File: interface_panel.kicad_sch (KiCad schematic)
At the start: 49 parts, among them J1 Conn_01x04_Pin, J5 Led, J7 Conn_02x05_Odd_Even, J8 `, Q1 BC547, Q2 BC547, U1 SM420561N, U2 ATmega328P-P, U4 SM420561N, U7 TTP223-BA6, U8 TTP223-BA6, U9 TTP223-BA6, Y1 Crystal

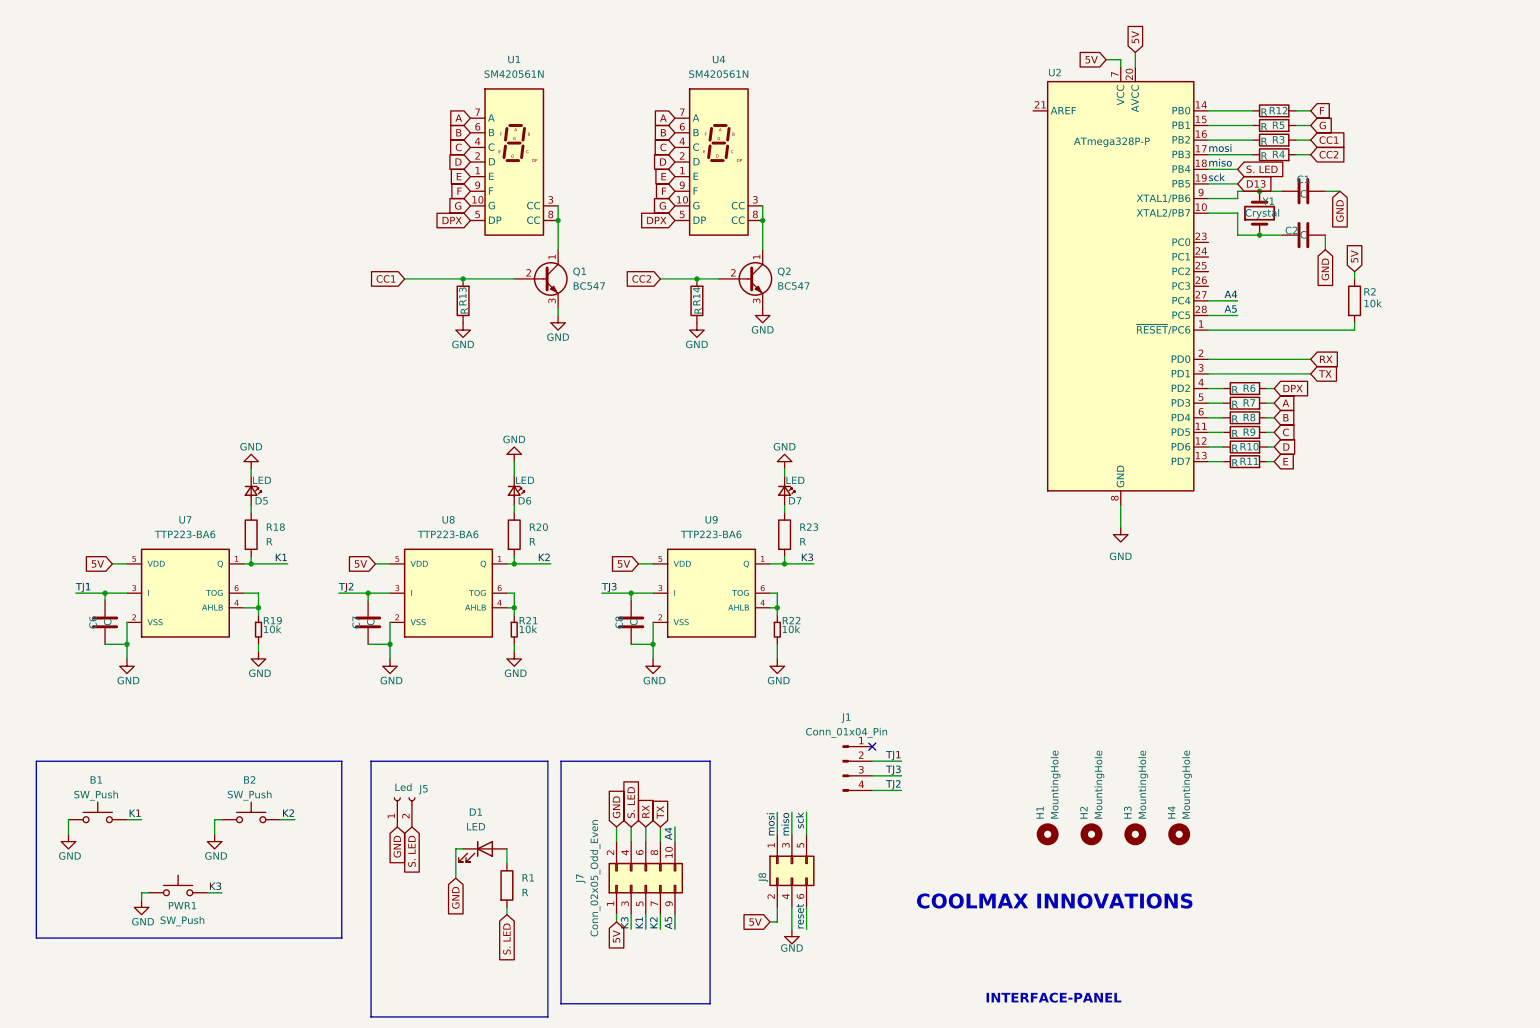
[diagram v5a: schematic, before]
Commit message: unrouted tracks - A4,A5
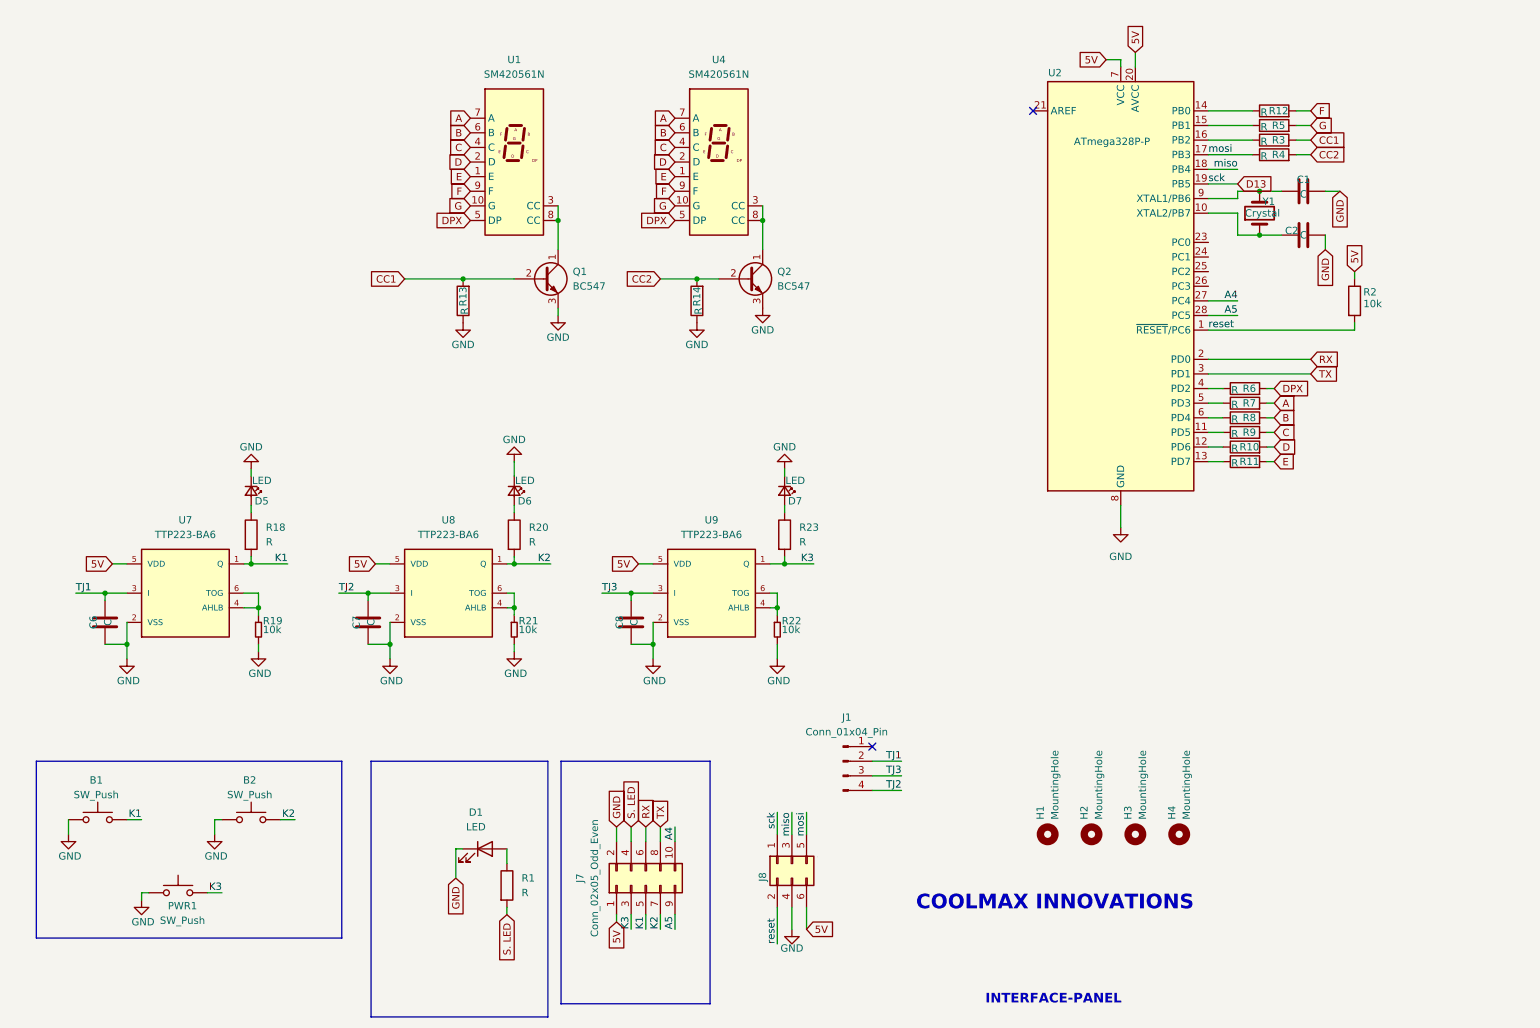
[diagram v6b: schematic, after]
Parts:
- removed J5: Led, Connector_JST:JST_EH_B2B-EH-A_1x02_P2.50mm_Vertical, symbol Connector:Conn_01x02_Socket
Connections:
- net 5V: now also J8.6 (Pin_6); no longer J8.2 (Pin_2)
- net D13: now also J8.1 (Pin_1); no longer J8.5 (Pin_5)
- net S. LED: no longer J8.3 (Pin_3), U2.18 (PB4)
- net mosi: now also J8.5 (Pin_5); no longer J8.1 (Pin_1)
- net reset: now also J8.2 (Pin_2), R2.2, U2.1 (~{RESET}/PC6); no longer J8.6 (Pin_6)
- new net miso: J8.3 (Pin_3), U2.18 (PB4)
- no-connect marks 1 -> 2
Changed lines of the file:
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@@
 		)
 	)
-	(rectangle
-		(start 86.36 158.75)
-		(end 86.36 158.75)
-		(stroke
-			(width 0)
-			(type default)
-		)
-		(fill
-			(type none)
-		)
-	)
 	(text "INTERFACE-PANEL\n"
 		(exclude_from_sim no)
@@
 		(at 170.18 146.05)
 	)
+	(no_connect
+		(at 198.12 35.56)
+	)
 	(wire
 		(pts
@@
 	(wire
 		(pts
+			(xy 233.68 45.72) (xy 228.6 45.72)
+		)
+		(stroke
+			(width 0)
+			(type default)
+		)
+	)
+	(wire
+		(pts
 			(xy 57.15 171.45) (xy 54.61 171.45)
 		)
@@
 	(wire
 		(pts
-			(xy 152.4 176.53) (xy 153.67 176.53)
-		)
-		(stroke
-			(width 0)
-			(type default)
-		)
-	)
-	(wire
-		(pts
 			(xy 69.85 158.75) (xy 67.31 158.75)
 		)
@@
 	(wire
 		(pts
-			(xy 153.67 176.53) (xy 153.67 173.99)
+			(xy 153.67 173.99) (xy 153.67 180.34)
 		)
 		(stroke
@@
 	(wire
 		(pts
-			(xy 228.6 45.72) (xy 233.68 45.72)
-		)
-		(stroke
-			(width 0)
-			(type default)
-		)
-	)
-	(wire
-		(pts
 			(xy 99.06 64.77) (xy 107.95 64.77)
 		)
@@
 		)
 	)
-	(label "mosi"
-		(at 153.67 157.48 270)
-		(effects
-			(font
-				(size 1.27 1.27)
-			)
-			(justify right bottom)
-		)
-	)
-	(label "sck"
-		(at 158.75 157.48 270)
+	(label "A4"
+		(at 135.89 160.02 270)
 		(effects
 			(font
@@
 		)
 	)
-	(label "A4"
-		(at 135.89 160.02 270)
+	(label "reset"
+		(at 153.67 180.34 90)
 		(effects
 			(font
 				(size 1.27 1.27)
 			)
-			(justify right bottom)
+			(justify left bottom)
 		)
 	)
@@
 		)
 	)
-	(label "K2"
-		(at 133.35 177.8 90)
+	(label "mosi"
+		(at 158.75 157.48 270)
 		(effects
 			(font
 				(size 1.27 1.27)
 			)
-			(justify left bottom)
+			(justify right bottom)
 		)
 	)
-	(label "miso"
-		(at 156.21 157.48 270)
+	(label "sck"
+		(at 153.67 157.48 270)
 		(effects
 			(font
@@
 		)
 	)
+	(label "K2"
+		(at 133.35 177.8 90)
+		(effects
+			(font
+				(size 1.27 1.27)
+			)
+			(justify left bottom)
+		)
+	)
 	(label "K1"
 		(at 68.58 114.3 180)
@@
 	)
 	(label "reset"
-		(at 158.75 177.8 90)
+		(at 228.6 73.66 0)
 		(effects
 			(font
@@
 	)
 	(label "miso"
-		(at 228.6 45.72 0)
+		(at 233.68 45.72 180)
 		(effects
 			(font
 				(size 1.27 1.27)
 			)
-			(justify left bottom)
+			(justify right bottom)
 		)
 	)
@@
 		)
 	)
+	(label "miso"
+		(at 156.21 157.48 270)
+		(effects
+			(font
+				(size 1.27 1.27)
+			)
+			(justify right bottom)
+		)
+	)
 	(label "TJ3"
 		(at 175.26 151.13 180)
@@
 		)
 	)
-	(global_label "S. LED"
-		(shape input)
-		(at 233.68 45.72 0)
-		(fields_autoplaced yes)
-		(effects
-			(font
-				(size 1.27 1.27)
-			)
-			(justify left)
-		)
-		(property "Intersheetrefs" "${INTERSHEET_REFS}"
-			(at 242.8942 45.72 0)
-			(effects
-				(font
-					(size 1.27 1.27)
-				)
-				(justify left)
-				(hide yes)
-			)
-		)
-	)
 	(global_label "RX"
 		(shape input)
@@
 	(global_label "5V"
 		(shape input)
-		(at 38.1 114.3 180)
+		(at 158.75 177.8 0)
 		(fields_autoplaced yes)
 		(effects
@@
 				(size 1.27 1.27)
 			)
-			(justify right)
+			(justify left)
 		)
 		(property "Intersheetrefs" "${INTERSHEET_REFS}"
-			(at 32.8167 114.3 0)
+			(at 164.0333 177.8 0)
 			(effects
 				(font
 					(size 1.27 1.27)
 				)
-				(justify right)
+				(justify left)
 				(hide yes)
 			)
@@
 	(global_label "5V"
 		(shape input)
-		(at 152.4 176.53 180)
+		(at 38.1 114.3 180)
 		(fields_autoplaced yes)
 		(effects
@@
 		)
 		(property "Intersheetrefs" "${INTERSHEET_REFS}"
-			(at 147.1167 176.53 0)
+			(at 32.8167 114.3 0)
 			(effects
 				(font
@@
 		)
 	)
-	(global_label "GND"
-		(shape input)
-		(at 87.63 160.02 270)
-		(fields_autoplaced yes)
-		(effects
-			(font
-				(size 1.27 1.27)
-			)
-			(justify right)
-		)
-		(property "Intersheetrefs" "${INTERSHEET_REFS}"
-			(at 87.63 166.8757 90)
-			(effects
-				(font
-					(size 1.27 1.27)
-				)
-				(justify right)
-				(hide yes)
-			)
-		)
-	)
 	(global_label "D"
 		(shape input)
@@
 		)
 	)
-	(global_label "S. LED"
-		(shape input)
-		(at 90.17 160.02 270)
-		(fields_autoplaced yes)
-		(effects
-			(font
-				(size 1.27 1.27)
-			)
-			(justify right)
-		)
-		(property "Intersheetrefs" "${INTERSHEET_REFS}"
-			(at 90.17 169.2342 90)
-			(effects
-				(font
-					(size 1.27 1.27)
-				)
-				(justify right)
-				(hide yes)
-			)
-		)
-	)
 	(global_label "G"
 		(shape input)
@@
 					(unit 1)
 				)
-			)
-		)
-	)
-	(symbol
-		(lib_id "Connector:Conn_01x02_Socket")
-		(at 87.63 154.94 90)
-		(unit 1)
-		(exclude_from_sim no)
-		(in_bom yes)
-		(on_board yes)
-		(dnp no)
-		(property "Reference" "J5"
-			(at 91.44 153.416 90)
-			(effects
-				(font
-					(size 1.27 1.27)
-				)
-				(justify right)
-			)
-		)
-		(property "Value" "Led"
-			(at 87.122 153.162 90)
-			(effects
-				(font
-					(size 1.27 1.27)
-				)
-				(justify right)
-			)
-		)
-		(property "Footprint" "Connector_JST:JST_EH_B2B-EH-A_1x02_P2.50mm_Vertical"
-			(at 87.63 154.94 0)
-			(effects
-				(font
-					(size 1.27 1.27)
-				)
-				(hide yes)
-			)
-		)
-		(property "Datasheet" "~"
-			(at 87.63 154.94 0)
-			(effects
-				(font
-					(size 1.27 1.27)
-				)
-				(hide yes)
-			)
-		)
-		(property "Description" "Generic connector, single row, 01x02, script generated"
-			(at 87.63 154.94 0)
-			(effects
-				(font
-					(size 1.27 1.27)
-				)
-				(hide yes)
-			)
-		)
-		(pin "2"
-		)
-		(pin "1"
-		)
-		(instances
-			(project "interface_panel"
-				(path "/9f0ac2f5-026e-46a7-84a3-e69ffa4f4cba"
-					(reference "J5")
-					(unit 1)
-				)

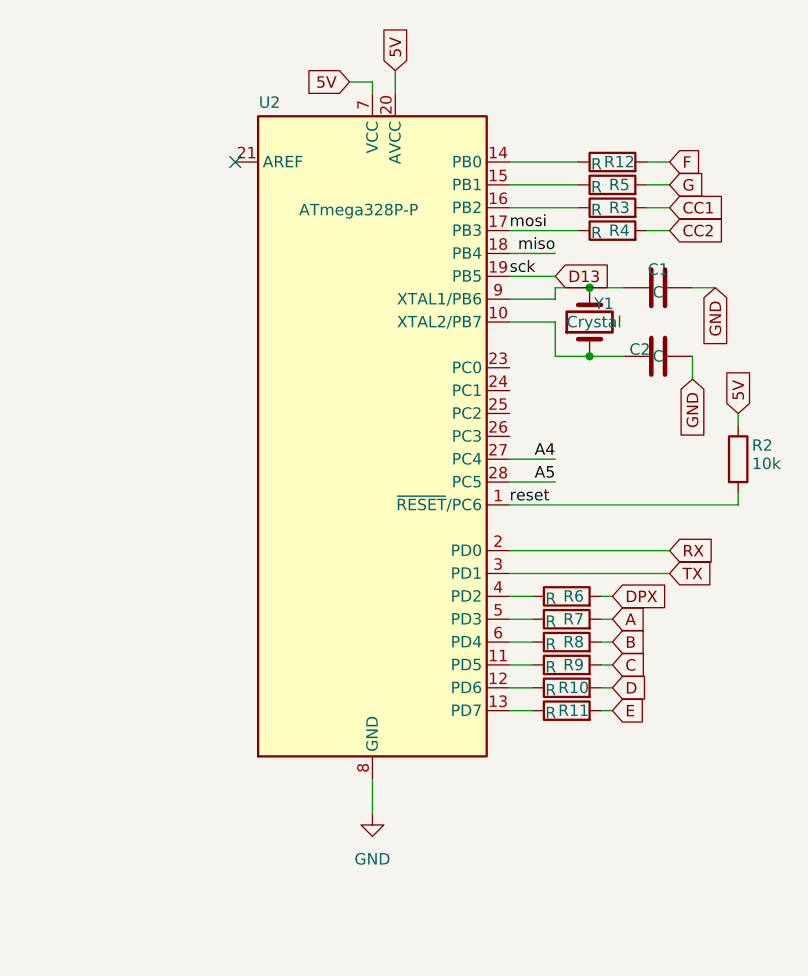
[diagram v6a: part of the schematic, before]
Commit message: Fixed- schematics -atmega symbol
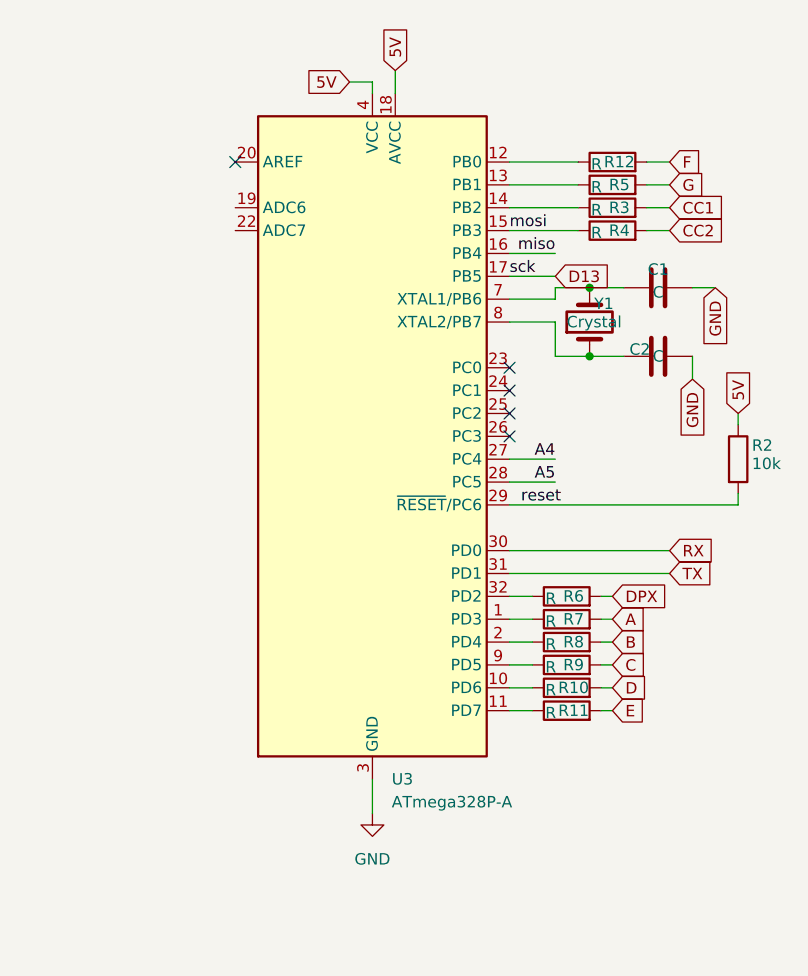
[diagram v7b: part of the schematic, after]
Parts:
- removed U2: ATmega328P-P, atmega328p-smd:QFP80P900X900X120-32N, symbol MCU_Microchip_ATmega:ATmega328P-P
- added U3: ATmega328P-A, Package_QFP:TQFP-32_7x7mm_P0.8mm, symbol MCU_Microchip_ATmega:ATmega328P-A
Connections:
- net 5V: now also U3.18 (AVCC), U3.4 (VCC), U3.6 (VCC)
- net A4: now also U3.27 (PC4)
- net A5: now also U3.28 (PC5)
- net D13: now also U3.17 (PB5)
- net GND: now also U3.21 (GND), U3.3 (GND), U3.5 (GND)
- net RX: now also U3.30 (PD0)
- net TX: now also U3.31 (PD1)
- net miso: now also U3.16 (PB4)
- net mosi: now also U3.15 (PB3)
- net reset: now also U3.29 (~{RESET}/PC6)
- net at R5.1: now also U3.13 (PB1)
- net at C1.1, Y1.2: now also U3.7 (XTAL1/PB6)
- net at R11.1: now also U3.11 (PD7)
- net at R7.1: now also U3.1 (PD3)
- net at R8.1: now also U3.2 (PD4)
- net at R10.1: now also U3.10 (PD6)
- net at R3.1: now also U3.14 (PB2)
- net at R9.1: now also U3.9 (PD5)
- net at C2.1, Y1.1: now also U3.8 (XTAL2/PB7)
- net at R12.1: now also U3.12 (PB0)
- net at R6.1: now also U3.32 (PD2)
- no-connect marks 2 -> 6
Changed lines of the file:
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@@
 	)
 	(no_connect
+		(at 228.6 60.96)
+	)
+	(no_connect
 		(at 170.18 146.05)
 	)
 	(no_connect
+		(at 228.6 66.04)
+	)
+	(no_connect
 		(at 198.12 35.56)
 	)
+	(no_connect
+		(at 228.6 58.42)
+	)
+	(no_connect
+		(at 228.6 63.5)
+	)
 	(wire
 		(pts
@@
 	(wire
 		(pts
+			(xy 228.6 73.66) (xy 254 73.66)
+		)
+		(stroke
+			(width 0)
+			(type default)
+		)
+	)
+	(wire
+		(pts
 			(xy 151.13 54.61) (xy 151.13 59.69)
 		)
@@
 	(wire
 		(pts
-			(xy 228.6 73.66) (xy 254 73.66)
-		)
-		(stroke
-			(width 0)
-			(type default)
-		)
-	)
-	(wire
-		(pts
 			(xy 158.75 157.48) (xy 158.75 161.29)
 		)
@@
 	)
 	(label "reset"
-		(at 228.6 73.66 0)
+		(at 229.87 73.66 0)
 		(effects
 			(font
@@
 	)
 	(symbol
+		(lib_id "MCU_Microchip_ATmega:ATmega328P-A")
+		(at 213.36 66.04 0)
+		(unit 1)
+		(exclude_from_sim no)
+		(in_bom yes)
+		(on_board yes)
+		(dnp no)
+		(fields_autoplaced yes)
+		(property "Reference" "U3"
+			(at 215.5033 104.14 0)
+			(effects
+				(font
+					(size 1.27 1.27)
+				)
+				(justify left)
+			)
+		)
+		(property "Value" "ATmega328P-A"
+			(at 215.5033 106.68 0)
+			(effects
+				(font
+					(size 1.27 1.27)
+				)
+				(justify left)
+			)
+		)
+		(property "Footprint" "Package_QFP:TQFP-32_7x7mm_P0.8mm"
+			(at 213.36 66.04 0)
+			(effects
+				(font
+					(size 1.27 1.27)
+					(italic yes)
+				)
+				(hide yes)
+			)
+		)
+		(property "Datasheet" "http://ww1.microchip.com/downloads/en/DeviceDoc/ATmega328_P%20AVR%20MCU%20with%20picoPower%20Technology%20Data%20Sheet%2040001984A.pdf"
+			(at 213.36 66.04 0)
+			(effects
+				(font
+					(size 1.27 1.27)
+				)
+				(hide yes)
+			)
+		)
+		(property "Description" "20MHz, 32kB Flash, 2kB SRAM, 1kB EEPROM, TQFP-32"
+			(at 213.36 66.04 0)
+			(effects
+				(font
+					(size 1.27 1.27)
+				)
+				(hide yes)
+			)
+		)
+		(pin "26"
+		)
+		(pin "14"
+		)
+		(pin "16"
+		)
+		(pin "31"
+		)
+		(pin "28"
+		)
+		(pin "1"
+		)
+		(pin "21"
+		)
+		(pin "32"
+		)
+		(pin "3"
+		)
+		(pin "18"
+		)
+		(pin "13"
+		)
+		(pin "25"
+		)
+		(pin "20"
+		)
+		(pin "5"
+		)
+		(pin "23"
+		)
+		(pin "15"
+		)
+		(pin "19"
+		)
+		(pin "8"
+		)
+		(pin "4"
+		)
+		(pin "6"
+		)
+		(pin "22"
+		)
+		(pin "12"
+		)
+		(pin "17"
+		)
+		(pin "7"
+		)
+		(pin "24"
+		)
+		(pin "27"
+		)
+		(pin "29"
+		)
+		(pin "30"
+		)
+		(pin "2"
+		)
+		(pin "10"
+		)
+		(pin "11"
+		)
+		(pin "9"
+		)
+		(instances
+			(project ""
+				(path "/9f0ac2f5-026e-46a7-84a3-e69ffa4f4cba"
+					(reference "U3")
+					(unit 1)
+				)
+			)
+		)
+	)
+	(symbol
 		(lib_id "Device:R")
 		(at 234.95 93.98 90)
@@
 					(unit 1)
 				)
-			)
-		)
-	)
-	(symbol
-		(lib_id "MCU_Microchip_ATmega:ATmega328P-P")
-		(at 213.36 66.04 0)
-		(unit 1)
-		(exclude_from_sim no)
-		(in_bom yes)
-		(on_board yes)
-		(dnp no)
-		(property "Reference" "U2"
-			(at 201.93 28.956 0)
-			(effects
-				(font
-					(size 1.27 1.27)
-				)
-			)
-		)
-		(property "Value" "ATmega328P-P"
-			(at 211.836 40.894 0)
-			(effects
-				(font
-					(size 1.27 1.27)
-				)
-			)
-		)
-		(property "Footprint" "atmega328p-smd:QFP80P900X900X120-32N"
-			(at 213.36 66.04 0)
-			(effects
-				(font
-					(size 1.27 1.27)
-					(italic yes)
-				)
-				(hide yes)
-			)
-		)
-		(property "Datasheet" "http://ww1.microchip.com/downloads/en/DeviceDoc/ATmega328_P%20AVR%20MCU%20with%20picoPower%20Technology%20Data%20Sheet%2040001984A.pdf"
-			(at 213.36 66.04 0)
-			(effects
-				(font
-					(size 1.27 1.27)
-				)
-				(hide yes)
-			)
-		)
-		(property "Description" "20MHz, 32kB Flash, 2kB SRAM, 1kB EEPROM, DIP-28"
-			(at 213.36 66.04 0)
-			(effects
-				(font
-					(size 1.27 1.27)
-				)
-				(hide yes)
-			)
-		)
-		(pin "1"
-		)
-		(pin "22"
-		)
-		(pin "11"
-		)
-		(pin "26"
-		)
-		(pin "19"
-		)
-		(pin "9"
-		)
-		(pin "15"
-		)
-		(pin "5"
-		)
-		(pin "20"
-		)
-		(pin "28"
-		)
-		(pin "25"
-		)
-		(pin "6"
-		)
-		(pin "3"
-		)
-		(pin "21"
-		)
-		(pin "8"
-		)
-		(pin "13"
-		)
-		(pin "24"
-		)
-		(pin "18"
-		)
-		(pin "17"
-		)
-		(pin "2"
-		)
-		(pin "27"
-		)
-		(pin "12"
-		)
-		(pin "10"
-		)
-		(pin "14"
-		)
-		(pin "7"
-		)
-		(pin "16"
-		)
-		(pin "4"
-		)
-		(pin "23"
-		)
-		(instances
-			(project "interface_panel"
-				(path "/9f0ac2f5-026e-46a7-84a3-e69ffa4f4cba"
-					(reference "U2")
-					(unit 1)
-				)
